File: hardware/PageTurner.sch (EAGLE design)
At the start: 11 parts

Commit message: Mic input routed to headphones works
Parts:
- added MAX9814: (no value), pinhead:PINHD-1X3
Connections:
- removed net N$18: U$1.3V3-1, U$2.VOL_3.3V
- new net 3.3V: MAX9814.2, U$1.3V3-1, U$2.3V
- new net GND: MAX9814.1, U$2.INGND1
- new net N$17: U$1.10-CS, U$2.10
- new net N$19: U$1.11-MOSI/CTX1, U$2.11
- new net N$20: U$1.12-MISO/MQSL, U$2.12
- new net N$21: U$1.13-SCK/CRX1/LED, U$2.13
- new net OUT: MAX9814.3, U$2.INL
- net N$7: now also U$2.G; no longer U$2.VOL_GND
- net N$9: now also U$1.5-IN2
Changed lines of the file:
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@@
 <part name="U$2" library="Teensy_Audioshield" deviceset="AUDIOSHIELD" device=""/>
 <part name="SW_REC" library="pinhead" library_urn="urn:adsk.eagle:library:325" deviceset="PINHD-1X2" device="" package3d_urn="urn:adsk.eagle:package:22435/2"/>
+<part name="MAX9814" library="pinhead" library_urn="urn:adsk.eagle:library:325" deviceset="PINHD-1X3" device="" package3d_urn="urn:adsk.eagle:package:22458/2"/>
 </parts>
 <sheets>
@@
 <attribute name="NAME" x="-57.15" y="13.335" size="1.778" layer="95"/>
 <attribute name="VALUE" x="-57.15" y="2.54" size="1.778" layer="96"/>
+</instance>
+<instance part="MAX9814" gate="A" x="205.74" y="43.18" smashed="yes">
+<attribute name="NAME" x="199.39" y="48.895" size="1.778" layer="95"/>
+<attribute name="VALUE" x="199.39" y="35.56" size="1.778" layer="96"/>
 </instance>
 </instances>
@@
 <junction x="-38.1" y="0"/>
 <pinref part="U$2" gate="AUDIO$1" pin="GND"/>
-<wire x1="144.78" y1="81.28" x2="132.08" y2="81.28" width="0.1524" layer="91"/>
+<wire x1="144.78" y1="81.28" x2="139.7" y2="81.28" width="0.1524" layer="91"/>
+<wire x1="139.7" y1="81.28" x2="132.08" y2="81.28" width="0.1524" layer="91"/>
 <wire x1="132.08" y1="81.28" x2="132.08" y2="0" width="0.1524" layer="91"/>
 <wire x1="132.08" y1="0" x2="104.14" y2="0" width="0.1524" layer="91"/>
 <junction x="104.14" y="0"/>
-<pinref part="U$2" gate="AUDIO$1" pin="VOL_GND"/>
-<wire x1="180.34" y1="33.02" x2="185.42" y2="33.02" width="0.1524" layer="91"/>
-<wire x1="185.42" y1="33.02" x2="185.42" y2="0" width="0.1524" layer="91"/>
 <wire x1="185.42" y1="0" x2="132.08" y2="0" width="0.1524" layer="91"/>
 <junction x="132.08" y="0"/>
@@
 <wire x1="96.52" y1="10.16" x2="96.52" y2="0" width="0.1524" layer="91"/>
 <junction x="96.52" y="0"/>
+<pinref part="U$2" gate="AUDIO$1" pin="G"/>
+<wire x1="139.7" y1="81.28" x2="139.7" y2="76.2" width="0.1524" layer="91"/>
+<wire x1="139.7" y1="76.2" x2="144.78" y2="76.2" width="0.1524" layer="91"/>
+<junction x="139.7" y="81.28"/>
 </segment>
 </net>
@@
 <pinref part="S_REC" gate="1" pin="P"/>
 <wire x1="-48.26" y1="17.78" x2="-48.26" y2="20.32" width="0.1524" layer="91"/>
-<wire x1="-48.26" y1="53.34" x2="-48.26" y2="20.32" width="0.1524" layer="91"/>
 <junction x="-48.26" y="20.32"/>
 <pinref part="SW_REC" gate="G$1" pin="1"/>
+<wire x1="-48.26" y1="30.48" x2="-48.26" y2="20.32" width="0.1524" layer="91"/>
 <wire x1="-48.26" y1="17.78" x2="-53.34" y2="17.78" width="0.1524" layer="91"/>
 <wire x1="-53.34" y1="17.78" x2="-53.34" y2="10.16" width="0.1524" layer="91"/>
 <junction x="-48.26" y="17.78"/>
+<pinref part="U$1" gate="G$1" pin="5-IN2"/>
+<wire x1="27.94" y1="30.48" x2="-48.26" y2="30.48" width="0.1524" layer="91"/>
 </segment>
 </net>
@@
 <pinref part="U$2" gate="AUDIO$1" pin="7"/>
 <wire x1="144.78" y1="53.34" x2="114.3" y2="53.34" width="0.1524" layer="91"/>
-<wire x1="114.3" y1="53.34" x2="114.3" y2="40.64" width="0.1524" layer="91"/>
+<wire x1="114.3" y1="53.34" x2="114.3" y2="35.56" width="0.1524" layer="91"/>
 <pinref part="U$1" gate="G$1" pin="7-OUT1A/RX2"/>
-<wire x1="114.3" y1="40.64" x2="83.82" y2="40.64" width="0.1524" layer="91"/>
-</segment>
-</net>
-<net name="N$18" class="0">
-<segment>
-<pinref part="U$1" gate="G$1" pin="3V3-1"/>
-<wire x1="68.58" y1="86.36" x2="68.58" y2="91.44" width="0.1524" layer="91"/>
-<wire x1="68.58" y1="91.44" x2="190.5" y2="91.44" width="0.1524" layer="91"/>
-<wire x1="190.5" y1="91.44" x2="190.5" y2="27.94" width="0.1524" layer="91"/>
-<pinref part="U$2" gate="AUDIO$1" pin="VOL_3.3V"/>
-<wire x1="190.5" y1="27.94" x2="180.34" y2="27.94" width="0.1524" layer="91"/>
+<wire x1="86.36" y1="40.64" x2="83.82" y2="40.64" width="0.1524" layer="91"/>
+<wire x1="86.36" y1="40.64" x2="86.36" y2="35.56" width="0.1524" layer="91"/>
+<wire x1="86.36" y1="35.56" x2="114.3" y2="35.56" width="0.1524" layer="91"/>
 </segment>
 </net>
@@
 </segment>
 </net>
+<net name="N$17" class="0">
+<segment>
+<pinref part="U$2" gate="AUDIO$1" pin="10"/>
+<wire x1="144.78" y1="45.72" x2="101.6" y2="45.72" width="0.1524" layer="91"/>
+<wire x1="101.6" y1="45.72" x2="101.6" y2="53.34" width="0.1524" layer="91"/>
+<pinref part="U$1" gate="G$1" pin="10-CS"/>
+<wire x1="101.6" y1="53.34" x2="83.82" y2="53.34" width="0.1524" layer="91"/>
+</segment>
+</net>
+<net name="N$19" class="0">
+<segment>
+<pinref part="U$1" gate="G$1" pin="11-MOSI/CTX1"/>
+<wire x1="83.82" y1="50.8" x2="99.06" y2="50.8" width="0.1524" layer="91"/>
+<wire x1="99.06" y1="50.8" x2="99.06" y2="43.18" width="0.1524" layer="91"/>
+<pinref part="U$2" gate="AUDIO$1" pin="11"/>
+<wire x1="99.06" y1="43.18" x2="144.78" y2="43.18" width="0.1524" layer="91"/>
+</segment>
+</net>
+<net name="N$20" class="0">
+<segment>
+<pinref part="U$1" gate="G$1" pin="12-MISO/MQSL"/>
+<wire x1="83.82" y1="48.26" x2="96.52" y2="48.26" width="0.1524" layer="91"/>
+<wire x1="96.52" y1="48.26" x2="96.52" y2="40.64" width="0.1524" layer="91"/>
+<pinref part="U$2" gate="AUDIO$1" pin="12"/>
+<wire x1="96.52" y1="40.64" x2="144.78" y2="40.64" width="0.1524" layer="91"/>
+</segment>
+</net>
+<net name="N$21" class="0">
+<segment>
+<pinref part="U$2" gate="AUDIO$1" pin="13"/>
+<wire x1="144.78" y1="38.1" x2="88.9" y2="38.1" width="0.1524" layer="91"/>
+<wire x1="88.9" y1="38.1" x2="88.9" y2="25.4" width="0.1524" layer="91"/>
+<pinref part="U$1" gate="G$1" pin="13-SCK/CRX1/LED"/>
+<wire x1="88.9" y1="25.4" x2="83.82" y2="25.4" width="0.1524" layer="91"/>
+</segment>
+</net>
+<net name="GND" class="0">
+<segment>
+<pinref part="MAX9814" gate="A" pin="1"/>
+<wire x1="203.2" y1="45.72" x2="190.5" y2="45.72" width="0.1524" layer="91"/>
+<label x="193.04" y="45.72" size="1.778" layer="95"/>
+<pinref part="U$2" gate="AUDIO$1" pin="INGND1"/>
+<wire x1="190.5" y1="45.72" x2="190.5" y2="81.28" width="0.1524" layer="91"/>
+<wire x1="190.5" y1="81.28" x2="180.34" y2="81.28" width="0.1524" layer="91"/>
+</segment>
+</net>
+<net name="3.3V" class="0">
+<segment>
+<pinref part="MAX9814" gate="A" pin="2"/>
+<wire x1="203.2" y1="43.18" x2="193.04" y2="43.18" width="0.1524" layer="91"/>
+<label x="193.04" y="43.18" size="1.778" layer="95"/>
+<pinref part="U$1" gate="G$1" pin="3V3-1"/>
+<wire x1="68.58" y1="86.36" x2="68.58" y2="91.44" width="0.1524" layer="91"/>
+<wire x1="68.58" y1="91.44" x2="134.62" y2="91.44" width="0.1524" layer="91"/>
+<pinref part="U$2" gate="AUDIO$1" pin="3V"/>
+<wire x1="144.78" y1="73.66" x2="134.62" y2="73.66" width="0.1524" layer="91"/>
+<wire x1="134.62" y1="73.66" x2="134.62" y2="86.36" width="0.1524" layer="91"/>
+<wire x1="134.62" y1="86.36" x2="134.62" y2="91.44" width="0.1524" layer="91"/>
+<wire x1="134.62" y1="86.36" x2="193.04" y2="86.36" width="0.1524" layer="91"/>
+<junction x="134.62" y="86.36"/>
+<wire x1="193.04" y1="86.36" x2="193.04" y2="43.18" width="0.1524" layer="91"/>
+</segment>
+</net>
+<net name="OUT" class="0">
+<segment>
+<pinref part="MAX9814" gate="A" pin="3"/>
+<wire x1="203.2" y1="40.64" x2="187.96" y2="40.64" width="0.1524" layer="91"/>
+<label x="193.04" y="40.64" size="1.778" layer="95"/>
+<wire x1="187.96" y1="40.64" x2="187.96" y2="76.2" width="0.1524" layer="91"/>
+<pinref part="U$2" gate="AUDIO$1" pin="INL"/>
+<wire x1="187.96" y1="76.2" x2="180.34" y2="76.2" width="0.1524" layer="91"/>
+</segment>
+</net>

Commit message: preparations for futrue improvements
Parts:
- removed LED_GREEN, LED_RED, LED_YELLOW: (no value), led:LED3MM
- removed R1, R2, R3: 470, rcl:R-EU_0207/12
- removed SW_REC: (no value), pinhead:PINHD-1X2
- removed S_REC: (no value), switch-omron:10-XX
- added BLUEFRUIT: (no value), pinhead:PINHD-1X4
- added SV1: (no value), con-lsta:FE08-1
- renumbered UART2USB to LOGOUTPUT
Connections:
- removed net N$13: U$1.20-A6/TX5/LRCLK1, U$2.20
- removed net N$14: U$1.19-A5/SCL0, U$2.19
- removed net N$15: U$1.7-OUT1A/RX2, U$2.7
- removed net N$16: U$1.18-A4/SDA0, U$2.18
- removed net N$17: U$1.10-CS, U$2.10
- removed net N$19: U$1.11-MOSI/CTX1, U$2.11
- removed net N$20: U$1.12-MISO/MQSL, U$2.12
- removed net N$21: U$1.13-SCK/CRX1/LED, U$2.13
- removed net N$4: LED_YELLOW.A, R3.1
- removed net N$7: LED_GREEN.C, LED_RED.C, LED_YELLOW.C, LOGOUTPUT.3, SW_REC.2, S_REC.S, S_REC.S1, U$1.GND1, U$2.G, U$2.GND
- new net 3V: MAX9814.2, U$2.3V
- new net BLE_RX: BLUEFRUIT.3, U$1.17-A3/TX4/SDA1
- new net BLE_TX: BLUEFRUIT.4, U$1.16-A2/RX4/SCL1
- net 3.3V: now also BLUEFRUIT.2; no longer MAX9814.2, U$2.3V
- net GND: now also BLUEFRUIT.1, LOGOUTPUT.3, SV1.1, U$1.GND1; no longer U$2.INGND1
- net N$1: now also SV1.2; no longer R1.2
- net N$11: now also SV1.5, U$1.5-IN2; no longer U$1.23-A9/CRX1/MCLK1, U$2.23
- net N$12: now also SV1.6, U$1.15-A1/RX3/SPDIF_IN; no longer U$1.21-A7/RX5/BCLK1, U$2.21
- net N$2: now also SV1.7; no longer R2.2, U$1.3-LRCLK2
- net N$3: now also SV1.8, U$1.9-OUT1C; no longer R3.2, U$1.4-BCLK1
- net N$5: now also U$1.14-A0/TX3/S-PDIF_IN; no longer LED_GREEN.A, R2.1
- net N$6: now also SV1.3, U$1.3-LRCLK2; no longer LED_RED.A, R1.1
- net N$9: now also SV1.4, U$1.4-BCLK1; no longer SW_REC.1, S_REC.P, S_REC.P1, U$1.5-IN2

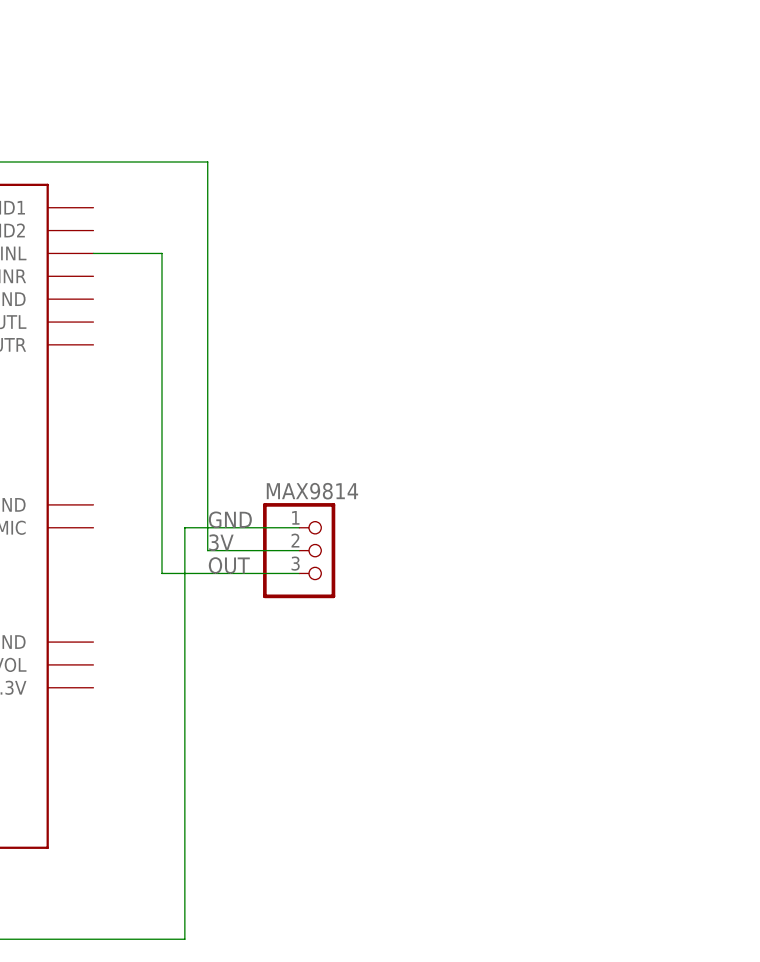
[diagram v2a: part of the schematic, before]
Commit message: separated some AI classes for better recall
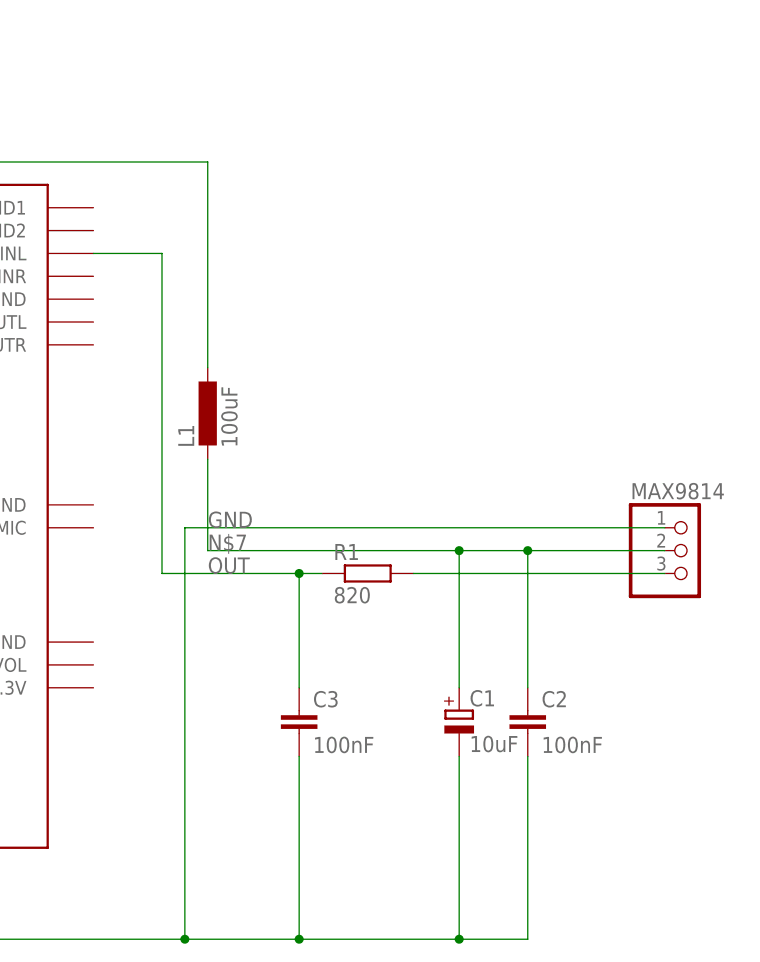
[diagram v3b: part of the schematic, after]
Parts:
- added C1: 10uF, rcl:CPOL-EUE2-4
- added C2, C3: 100nF, rcl:C-EU025-040X050
- added L1: 100uF, rcl:L-EU0207/5V
- added R1: 820, rcl:R-EU_0207/7
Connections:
- new net N$4: MAX9814.3, R1.2
- new net N$7: C1.+, C2.1, L1.2, MAX9814.2
- net 3V: now also L1.1; no longer MAX9814.2
- net GND: now also C1.-, C2.2, C3.2
- net OUT: now also C3.1, R1.1; no longer MAX9814.3
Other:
- moved on the sheet: MAX9814
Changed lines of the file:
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@@
 <part name="BLUEFRUIT" library="pinhead" library_urn="urn:adsk.eagle:library:325" deviceset="PINHD-1X4" device="" package3d_urn="urn:adsk.eagle:package:22407/2"/>
 <part name="SV1" library="con-lsta" library_urn="urn:adsk.eagle:library:161" deviceset="FE08-1" device="" package3d_urn="urn:adsk.eagle:package:8194/1"/>
+<part name="R1" library="rcl" library_urn="urn:adsk.eagle:library:334" deviceset="R-EU_" device="0207/7" package3d_urn="urn:adsk.eagle:package:23493/2" value="820"/>
+<part name="C1" library="rcl" library_urn="urn:adsk.eagle:library:334" deviceset="CPOL-EU" device="E2-4" package3d_urn="urn:adsk.eagle:package:23347/1" value="10uF"/>
+<part name="C2" library="rcl" library_urn="urn:adsk.eagle:library:334" deviceset="C-EU" device="025-040X050" package3d_urn="urn:adsk.eagle:package:23634/1" value="100nF"/>
+<part name="L1" library="rcl" library_urn="urn:adsk.eagle:library:334" deviceset="L-EU" device="0207/5V" package3d_urn="urn:adsk.eagle:package:23502/1" value="100uF"/>
+<part name="C3" library="rcl" library_urn="urn:adsk.eagle:library:334" deviceset="C-EU" device="025-040X050" package3d_urn="urn:adsk.eagle:package:23634/1" value="100nF"/>
 </parts>
 <sheets>
@@
 </instance>
 <instance part="U$2" gate="AUDIO$1" x="162.56" y="45.72" smashed="yes"/>
-<instance part="MAX9814" gate="A" x="205.74" y="43.18" smashed="yes">
-<attribute name="NAME" x="199.39" y="48.895" size="1.778" layer="95"/>
-<attribute name="VALUE" x="199.39" y="35.56" size="1.778" layer="96"/>
+<instance part="MAX9814" gate="A" x="246.38" y="43.18" smashed="yes">
+<attribute name="NAME" x="240.03" y="48.895" size="1.778" layer="95"/>
+<attribute name="VALUE" x="240.03" y="35.56" size="1.778" layer="96"/>
 </instance>
 <instance part="BLUEFRUIT" gate="A" x="-17.78" y="101.6" smashed="yes" rot="R180">
@@
 <attribute name="VALUE" x="-1.27" y="38.1" size="1.778" layer="96"/>
 <attribute name="NAME" x="-1.27" y="64.262" size="1.778" layer="95"/>
+</instance>
+<instance part="R1" gate="G$1" x="210.82" y="40.64" smashed="yes">
+<attribute name="NAME" x="207.01" y="42.1386" size="1.778" layer="95"/>
+<attribute name="VALUE" x="207.01" y="37.338" size="1.778" layer="96"/>
+</instance>
+<instance part="C1" gate="G$1" x="220.98" y="25.4" smashed="yes">
+<attribute name="NAME" x="222.123" y="25.8826" size="1.778" layer="95"/>
+<attribute name="VALUE" x="222.123" y="20.8026" size="1.778" layer="96"/>
+</instance>
+<instance part="C2" gate="G$1" x="228.6" y="25.4" smashed="yes">
+<attribute name="NAME" x="230.124" y="25.781" size="1.778" layer="95"/>
+<attribute name="VALUE" x="230.124" y="20.701" size="1.778" layer="96"/>
+</instance>
+<instance part="L1" gate="G$1" x="193.04" y="58.42" smashed="yes">
+<attribute name="NAME" x="191.5414" y="54.61" size="1.778" layer="95" rot="R90"/>
+<attribute name="VALUE" x="196.342" y="54.61" size="1.778" layer="96" rot="R90"/>
+</instance>
+<instance part="C3" gate="G$1" x="203.2" y="25.4" smashed="yes">
+<attribute name="NAME" x="204.724" y="25.781" size="1.778" layer="95"/>
+<attribute name="VALUE" x="204.724" y="20.701" size="1.778" layer="96"/>
 </instance>
 </instances>
@@
 <segment>
 <pinref part="MAX9814" gate="A" pin="1"/>
-<wire x1="203.2" y1="45.72" x2="190.5" y2="45.72" width="0.1524" layer="91"/>
+<wire x1="243.84" y1="45.72" x2="190.5" y2="45.72" width="0.1524" layer="91"/>
 <label x="193.04" y="45.72" size="1.778" layer="95"/>
 <wire x1="190.5" y1="45.72" x2="190.5" y2="0" width="0.1524" layer="91"/>
@@
 <wire x1="10.16" y1="43.18" x2="10.16" y2="0" width="0.1524" layer="91"/>
 <junction x="10.16" y="0"/>
+<pinref part="C1" gate="G$1" pin="-"/>
+<wire x1="220.98" y1="20.32" x2="220.98" y2="0" width="0.1524" layer="91"/>
+<wire x1="220.98" y1="0" x2="203.2" y2="0" width="0.1524" layer="91"/>
+<junction x="190.5" y="0"/>
+<pinref part="C2" gate="G$1" pin="2"/>
+<wire x1="203.2" y1="0" x2="190.5" y2="0" width="0.1524" layer="91"/>
+<wire x1="228.6" y1="20.32" x2="228.6" y2="0" width="0.1524" layer="91"/>
+<wire x1="228.6" y1="0" x2="220.98" y2="0" width="0.1524" layer="91"/>
+<junction x="220.98" y="0"/>
+<pinref part="C3" gate="G$1" pin="2"/>
+<wire x1="203.2" y1="20.32" x2="203.2" y2="0" width="0.1524" layer="91"/>
+<junction x="203.2" y="0"/>
 </segment>
 </net>
@@
 <net name="OUT" class="0">
 <segment>
-<pinref part="MAX9814" gate="A" pin="3"/>
-<wire x1="203.2" y1="40.64" x2="187.96" y2="40.64" width="0.1524" layer="91"/>
 <label x="193.04" y="40.64" size="1.778" layer="95"/>
 <wire x1="187.96" y1="40.64" x2="187.96" y2="76.2" width="0.1524" layer="91"/>
 <pinref part="U$2" gate="AUDIO$1" pin="INL"/>
 <wire x1="187.96" y1="76.2" x2="180.34" y2="76.2" width="0.1524" layer="91"/>
+<pinref part="R1" gate="G$1" pin="1"/>
+<wire x1="187.96" y1="40.64" x2="203.2" y2="40.64" width="0.1524" layer="91"/>
+<pinref part="C3" gate="G$1" pin="1"/>
+<wire x1="203.2" y1="40.64" x2="205.74" y2="40.64" width="0.1524" layer="91"/>
+<wire x1="203.2" y1="40.64" x2="203.2" y2="27.94" width="0.1524" layer="91"/>
+<junction x="203.2" y="40.64"/>
 </segment>
 </net>
@@
 <net name="3V" class="0">
 <segment>
-<pinref part="MAX9814" gate="A" pin="2"/>
-<wire x1="203.2" y1="43.18" x2="193.04" y2="43.18" width="0.1524" layer="91"/>
 <pinref part="U$2" gate="AUDIO$1" pin="3V"/>
 <wire x1="144.78" y1="73.66" x2="139.7" y2="73.66" width="0.1524" layer="91"/>
 <wire x1="139.7" y1="73.66" x2="139.7" y2="86.36" width="0.1524" layer="91"/>
 <wire x1="139.7" y1="86.36" x2="193.04" y2="86.36" width="0.1524" layer="91"/>
-<wire x1="193.04" y1="86.36" x2="193.04" y2="43.18" width="0.1524" layer="91"/>
-<label x="193.04" y="43.18" size="1.778" layer="95"/>
+<wire x1="193.04" y1="86.36" x2="193.04" y2="63.5" width="0.1524" layer="91"/>
+<pinref part="L1" gate="G$1" pin="1"/>
 </segment>
 </net>
@@
 <pinref part="SV1" gate="G$1" pin="7"/>
 <wire x1="7.62" y1="58.42" x2="17.78" y2="58.42" width="0.1524" layer="91"/>
+</segment>
+</net>
+<net name="N$4" class="0">
+<segment>
+<pinref part="MAX9814" gate="A" pin="3"/>
+<wire x1="243.84" y1="40.64" x2="215.9" y2="40.64" width="0.1524" layer="91"/>
+<pinref part="R1" gate="G$1" pin="2"/>
+</segment>
+</net>
+<net name="N$7" class="0">
+<segment>
+<wire x1="193.04" y1="53.34" x2="193.04" y2="43.18" width="0.1524" layer="91"/>
+<wire x1="220.98" y1="43.18" x2="193.04" y2="43.18" width="0.1524" layer="91"/>
+<pinref part="C1" gate="G$1" pin="+"/>
+<wire x1="220.98" y1="27.94" x2="220.98" y2="43.18" width="0.1524" layer="91"/>
+<junction x="220.98" y="43.18"/>
+<pinref part="MAX9814" gate="A" pin="2"/>
+<wire x1="243.84" y1="43.18" x2="228.6" y2="43.18" width="0.1524" layer="91"/>
+<wire x1="228.6" y1="43.18" x2="220.98" y2="43.18" width="0.1524" layer="91"/>
+<junction x="228.6" y="43.18"/>
+<pinref part="C2" gate="G$1" pin="1"/>
+<wire x1="228.6" y1="27.94" x2="228.6" y2="43.18" width="0.1524" layer="91"/>
+<label x="193.04" y="43.18" size="1.778" layer="95"/>
+<pinref part="L1" gate="G$1" pin="2"/>
 </segment>
 </net>
@@
 packages will not be understood (or retained) with this version.
 </note>
+<note version="8.4" severity="warning">
+Since Version 8.4, EAGLE supports properties for SPICE simulation.
+Probes in schematics and SPICE mapping objects found in parts and library devices
+will not be understood with this version. Update EAGLE to the latest version
+for full support of SPICE simulation.
+</note>
 </compatibility>
